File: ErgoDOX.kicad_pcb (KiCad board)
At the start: 2 copper layers, 182.8 x 158.9 mm, 77 parts, among them J1 USB, J2 3.5mm, J3 JMP, J4 JMP, SW0:10 SW0:3, SW0:11 SW0:2, SW0:12 SW0:1, SW0:7 SW0:6, SW0:8 SW0:5, SW0:9 SW0:4, SW1:10 SW1:3, SW1:11 SW1:2, SW1:12 SW1:1, SW1:13 SW1:0, SW1:9 SW1:4, SW2:10 SW2:3, SW2:11 SW2:2, SW2:12 SW2:1, SW2:13 SW2:0, SW2:7 SW2:6, SW2:8 SW2:5, SW2:9 SW2:4, SW3:10 SW3:3, SW3:11 SW3:2, SW3:12 SW3:1, SW3:13 SW3:0, SW3:8 SW3:5, SW3:9 SW3:4, SW4:10 SW4:3, SW4:11 SW4:2, SW4:12 SW4:1, SW4:13 SW4:0, SW4:7 SW4:6, SW4:8 SW4:5, SW4:9 SW4:4, SW5:10 SW5:3, SW5:11 SW5:2, SW5:12 SW5:1, SW5:13 SW5:0, SW5:7 SW5:6, SW5:8 SW5:5, SW5:9 SW5:4, U1 TEENSY2.0, U2 MCP23018

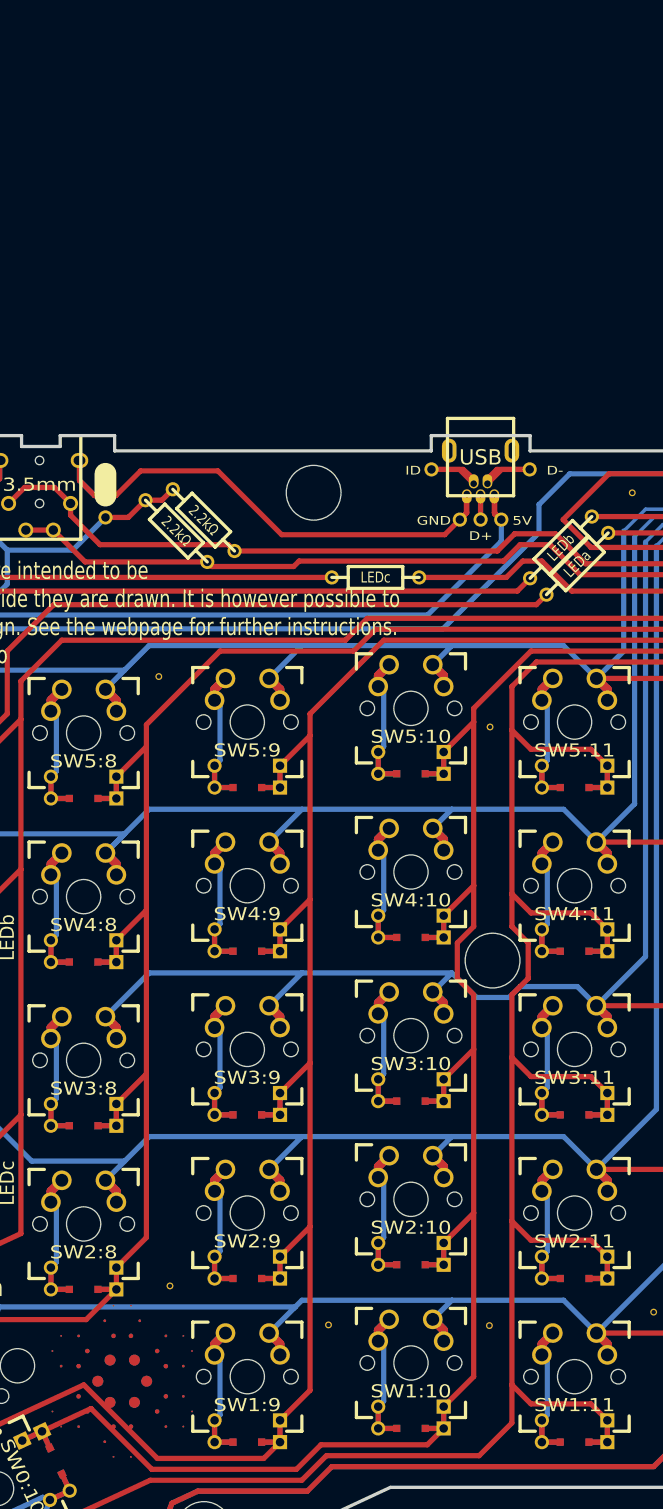
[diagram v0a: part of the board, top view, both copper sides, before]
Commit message: Assign footprints to old and new components.
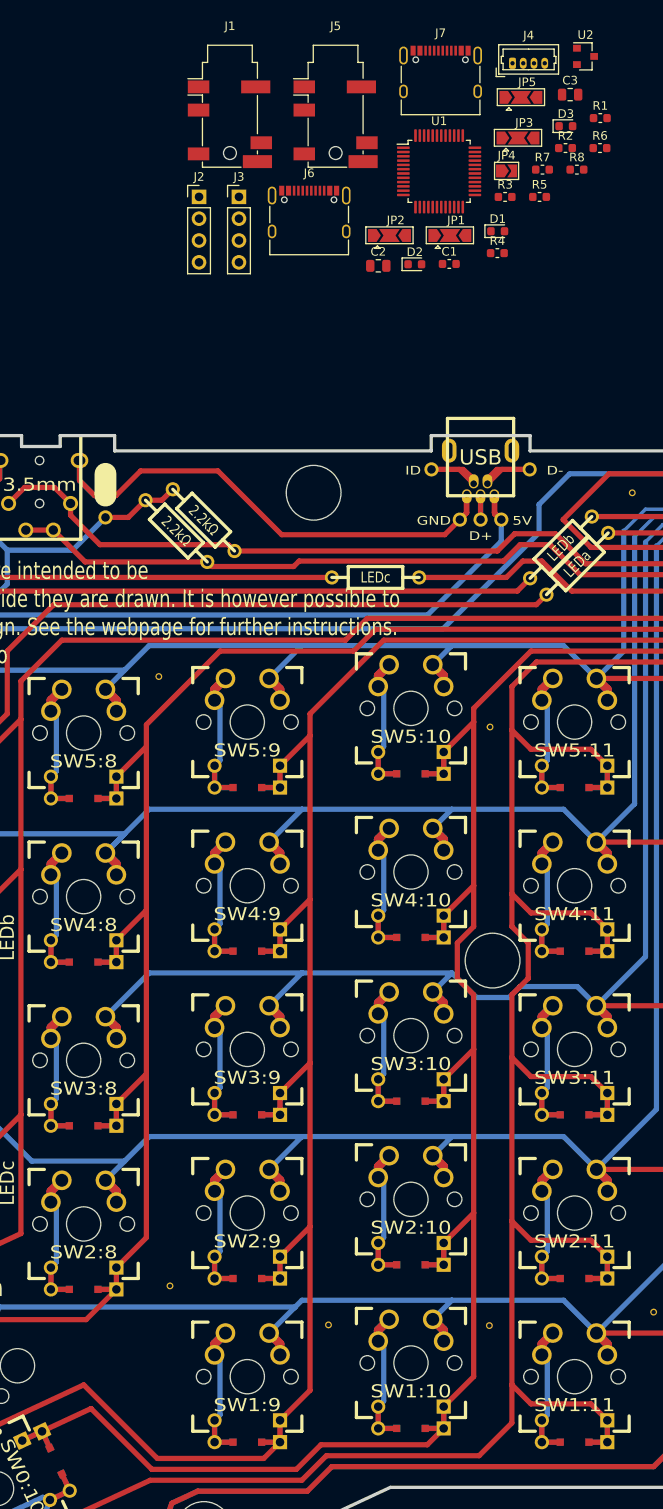
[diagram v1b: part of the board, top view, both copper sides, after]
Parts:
- removed STAR_1: STAR_FRONT, ErgoDOX pcb:STAR
- removed STAR_2: STAR_BACK, ErgoDOX pcb:STAR
- added C1: 100n, Capacitor_SMD:C_0603_1608Metric, F.Cu at (134.0, 10.5)
- added C2: C, Capacitor_SMD:C_0805_2012Metric, F.Cu at (125.7, 10.7)
- added C3: C, Capacitor_SMD:C_0805_2012Metric, F.Cu at (148.1, -9.21)
- added D1: LED, LED_SMD:LED_0603_1608Metric, F.Cu at (139.6, 6.69)
- added D2: LED, LED_SMD:LED_0603_1608Metric, F.Cu at (130.0, 10.5)
- added D3: LED, LED_SMD:LED_0603_1608Metric, F.Cu at (147.6, -5.54)
- added J1: SPLIT_JACK_TOP, Connector_Audio:Jack_3.5mm_PJ31060-I_Horizontal, F.Cu at (108.5, -5.76)
- added J2: EXT1_TOP, Connector_PinHeader_2.54mm:PinHeader_1x04_P2.54mm_Vertical, F.Cu at (104.9, 2.69)
- added J3: EXT1_BOT, Connector_PinHeader_2.54mm:PinHeader_1x04_P2.54mm_Vertical, F.Cu at (109.5, 2.69)
- added J4: EXT1_TOP2, Connector_Molex:Molex_PicoBlade_53047-0410_1x04_P1.25mm_Vertical, F.Cu at (141.4, -12.9)
- added J5: SPLIT_JACK_BOT, Connector_Audio:Jack_3.5mm_PJ31060-I_Horizontal, F.Cu at (120.8, -5.76)
- added J6: USB_C_TOP, Connector_USB:USB_C_Receptacle_XKB_U262-16XN-4BVC11, F.Cu at (117.7, 5.64)
- added J7: USB_C_BOT, Connector_USB:USB_C_Receptacle_XKB_U262-16XN-4BVC11, F.Cu at (133.0, -10.7)
- added JP1: EXT1_PWR, Jumper:SolderJumper-3_P2.0mm_Open_TrianglePad1.0x1.5mm, F.Cu at (134.1, 7.19)
- added JP2: SPLIT_PWR, Jumper:SolderJumper-3_P2.0mm_Open_TrianglePad1.0x1.5mm, F.Cu at (127.0, 7.19)
- added JP3: EXT1_PULL, Jumper:SolderJumper-3_P2.0mm_Open_TrianglePad1.0x1.5mm, F.Cu at (142.0, -4.16)
- added JP4: LR, Jumper:SolderJumper-2_P1.3mm_Open_TrianglePad1.0x1.5mm, F.Cu at (140.7, -0.33)
- added JP5: SPLIT_PULL, Jumper:SolderJumper-3_P2.0mm_Open_TrianglePad1.0x1.5mm, F.Cu at (142.3, -8.89)
- added R1: 1k, Resistor_SMD:R_0603_1608Metric, F.Cu at (151.6, -6.48)
- added R2: 2k, Resistor_SMD:R_0603_1608Metric, F.Cu at (147.5, -2.99)
- added R3: 2k, Resistor_SMD:R_0603_1608Metric, F.Cu at (140.5, 2.70)
- added R4: 2k, Resistor_SMD:R_0603_1608Metric, F.Cu at (139.6, 9.24)
- added R5: 2k, Resistor_SMD:R_0603_1608Metric, F.Cu at (144.5, 2.70)
- added R6: R, Resistor_SMD:R_0603_1608Metric, F.Cu at (151.5, -2.99)
- added R7: R, Resistor_SMD:R_0603_1608Metric, F.Cu at (144.8, -0.48)
- added R8: R, Resistor_SMD:R_0603_1608Metric, F.Cu at (148.9, -0.48)
- added U1: STM32F072C8Tx, Package_QFP:LQFP-48_7x7mm_P0.5mm, F.Cu at (132.8, -0.28)
- added U2: MCP1700-1202E_SOT23, Package_TO_SOT_SMD:SOT-23, F.Cu at (149.9, -13.7)
